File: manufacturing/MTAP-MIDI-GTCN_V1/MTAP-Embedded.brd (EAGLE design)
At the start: 160 x 100 mm, 32 parts, among them IC1 ESP32-WROOM-32D, IC2 AMS1117-3.3, X1 USB4140-GF-0230-C

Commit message: upd Embedded
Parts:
- added R11: 0R, rcl_GruS:R0805
- IC1: value ESP32-WROOM-32D -> ESP32-WROOM-32UE-N8; device modul_GruS:ESP32WROOM32D4MBPS -> modul_GruS:ESP32WROOM32UEN8
- R7: value (none) -> 47k5
- R8: value (none) -> 22k1
- S1, S2: device switch_GruS:STS6X -> switch_GruS:WE_436331045822
- moved H1 33.4 mm to (51.1, 46.0), turned to 270 degrees
- moved R1 29.7 mm to (47.3, 46.0)
- moved S2 23.9 mm to (37.5, 54.0), turned to 180 degrees
- moved C6 17.1 mm to (32.4, 53.3), flipped to the bottom, turned to 270 degrees
- moved C3 17.0 mm to (44.8, 14.0), flipped to the bottom, turned to 270 degrees
- moved C7 16.9 mm to (41.3, 49.8), flipped to the bottom, turned to 180 degrees
- moved S1 16.9 mm to (37.5, 54.0), flipped to the bottom, turned to 180 degrees
- moved C4 12.0 mm to (47.3, 14.0), flipped to the bottom
- moved V3 10.2 mm to (44.1, 40.0), turned to 270 degrees
- moved D2 8.58 mm to (44.1, 43.5), turned to 90 degrees
- moved C2 8.31 mm to (47.3, 43.2), turned to 0 degrees
- moved C1 8.26 mm to (51.1, 43.2), turned to 0 degrees
- moved R7 8.11 mm to (28.3, 44.5), turned to 90 degrees
- moved R3 7.55 mm to (40.6, 39.1), turned to 0 degrees
- moved IC2 7.31 mm to (49.2, 37.8)
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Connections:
- net GND: now also R11.2
- net PGND: now also R11.1
- net USB_DN: now also D4.1, X1.B5; no longer D3.1, X1.A5
- net USB_DP: now also D3.1, X1.A5; no longer D4.1, X1.B5
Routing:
- net +3V3: track 18.1 -> 70.8 mm
- net EN: track 6.68 -> 54.0 mm, vias 0 -> 4
- net GPIO0: track 4.32 -> 29.8 mm, vias 0 -> 1
- net VBUS: track 5.50 -> 29.7 mm
- net GND: track 14.1 -> 24.1 mm, vias 0 -> 13
- net USB_DP: track 3.85 -> 13.0 mm
- net RTS: track 3.24 -> 10.6 mm
- net N$16: track 10.0 -> 3.18 mm, vias 2 -> 0
- net RXD: track 12.6 -> 5.84 mm
- net TXD: track 14.9 -> 9.44 mm
- net RXD0: track 32.2 -> 26.8 mm, vias 2 -> 0
- net USB_DN: track 8.80 -> 13.6 mm
- net TXD0: track 29.7 -> 25.0 mm
- net N$4: track 4.59 -> 0.00 mm
- net DTR: track 21.7 -> 17.5 mm
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- added copper zone on layer 16, net GND
- added copper zone on layer 16, net PGND
- removed copper zone on layer 16, net +3V3
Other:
- board outline removed

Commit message: upd embedded schematic
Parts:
- moved R7 3.86 mm to (32.1, 45.1)
- moved C6 3.55 mm to (33.0, 49.8), turned to 180 degrees
- moved C3 1.31 mm to (44.5, 15.2), turned to 90 degrees
- moved C4 1.31 mm to (47.0, 15.2), turned to 90 degrees
- moved R10 0.63 mm to (33.0, 41.9)
- moved C8 0.32 mm to (36.5, 49.2)
- moved C9 0.32 mm to (34.3, 49.2)
- moved R8 0.32 mm to (32.1, 49.2)
- moved R9 0.32 mm to (34.3, 45.1)
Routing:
- net N$2: track 0.00 -> 6.67 mm
- net VBUS: track 29.7 -> 33.4 mm
- net N$3: track 0.00 -> 2.78 mm
- net +5V: track 6.37 -> 8.91 mm
- net GPIO0: track 29.8 -> 27.7 mm
- net PGND: track 3.40 -> 5.40 mm, vias 11 -> 32
- net N$4: track 0.00 -> 1.93 mm
- net +3V3: track 70.8 -> 72.6 mm
- net GND: vias 13 -> 15
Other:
- board outline added: 37.5 x 44.5 mm

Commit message: upd board
upd pcb
added Kostenrechnung
upd PPL-GruS
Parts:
- moved C3 11.8 mm to (56.2, 15.9), flipped to the top
- moved R11 9.40 mm to (58.4, 36.8)
- moved C4 7.01 mm to (54.0, 15.9), flipped to the top
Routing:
- net GND: track 24.1 -> 9.27 mm, vias 15 -> 14
- net EN: track 53.6 -> 58.6 mm
- net +3V3: track 72.6 -> 71.5 mm, vias 5 -> 4
- net PGND: vias 32 -> 25
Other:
- board size 37.5 x 44.5 mm -> 35.2 x 44.5 mm

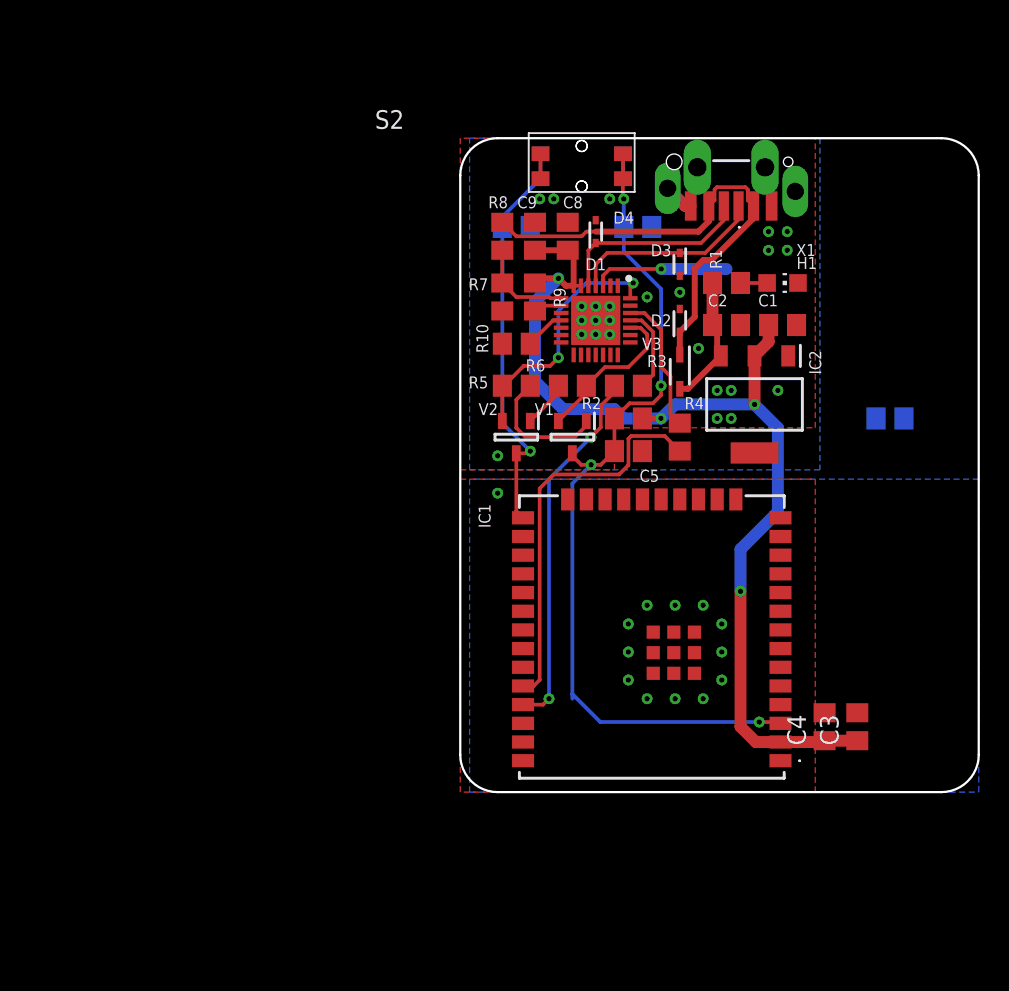
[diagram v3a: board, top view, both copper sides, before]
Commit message: Update Embedded
added PCM ADC to PCB
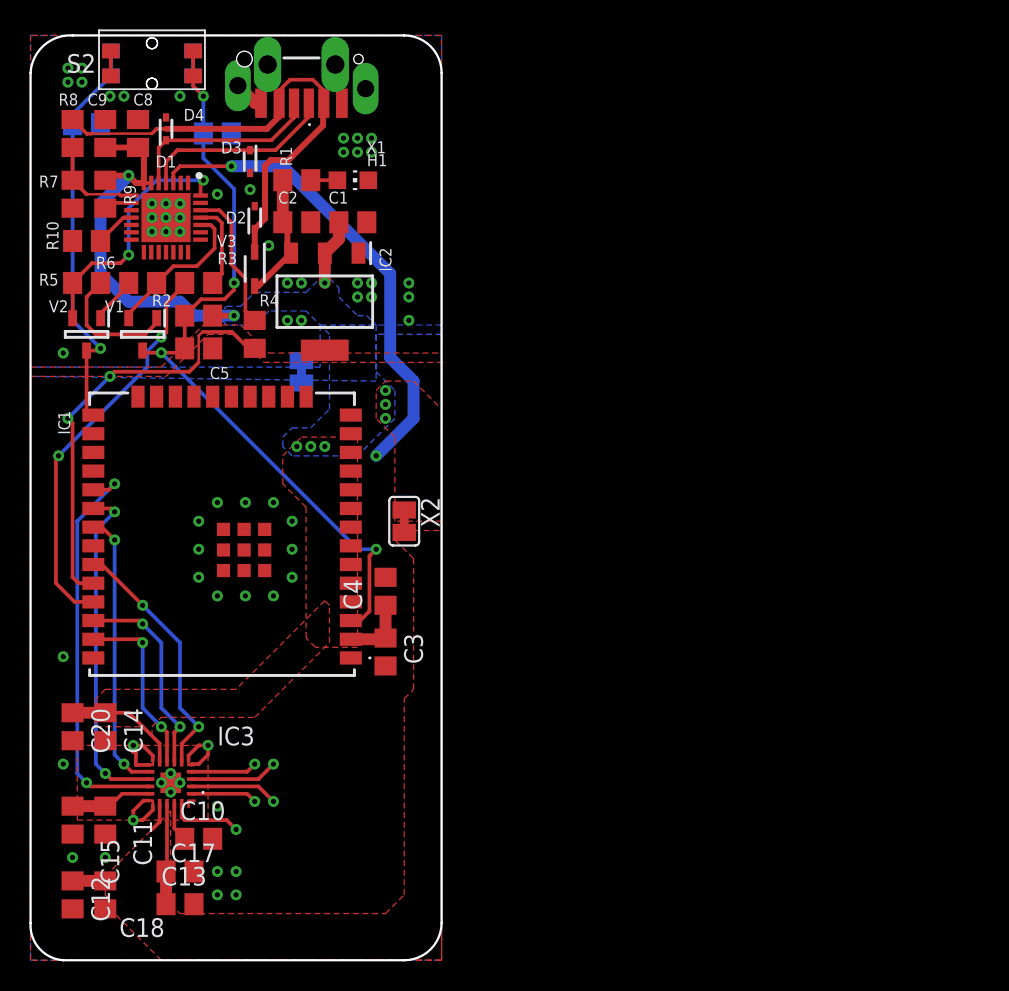
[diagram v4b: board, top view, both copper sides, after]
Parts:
- added C10, C12: 1u, rcl_GruS:C0805
- added C11, C13, C14: 10u, rcl_GruS:C0805
- added C15, C17, C18, C20: 100n, rcl_GruS:C0805
- added IC3: PCM1821IRTER, adc-dac_GruS:WQFN20
- added X2: (no value), con_GruS:MYLIB_SJ-SHORT
- C3, C5: value (none) -> 100n/50V
- C6, C7: value (none) -> 100n
- R10, R2, R5, R6: value (none) -> 10k
- R11: device rcl_GruS:R0805 -> con_GruS:MYLIB_SJ-SHORT
- R3, R4: value (none) -> 0R
- R9: value (none) -> 2k
- moved R11 40.1 mm to (18.4, 40.0), turned to 270 degrees
- moved C3 32.5 mm to (24.1, 21.0), turned to 270 degrees
- moved C4 31.2 mm to (24.1, 25.1)
- moved C6 30.0 mm to (3.81, 56.8)
- moved R10 30.0 mm to (3.81, 48.9)
- moved R5 30.0 mm to (3.81, 46.0)
- moved V2 30.0 mm to (3.81, 42.5)
- moved C1 30.0 mm to (21.9, 50.2)
- moved C5 30.0 mm to (11.4, 41.6)
- moved C8 30.0 mm to (7.30, 56.2)
- moved C9 30.0 mm to (5.08, 56.2)
- moved D3 30.0 mm to (14.9, 54.3)
- moved H1 30.0 mm to (21.9, 53.0)
- moved IC1 30.0 mm to (13.0, 29.2)
- moved R2 30.0 mm to (11.4, 43.8)
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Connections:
- new net AVDD: C12.1, C18.1, IC3.16, X2.2
- new net BCLK: IC1.36, IC3.7
- new net FSYNC: IC1.37, IC3.8
- new net FTM0: IC3.19
- new net GPIO12: IC1.14
- new net GPIO13: IC1.16
- new net GPIO14: IC1.13
- new net GPIO15: IC1.23
- new net GPIO16: IC1.27
- new net GPIO17: IC1.28
- new net GPIO2: IC1.24
- new net GPIO25: IC1.10
- new net GPIO26: IC1.11
- new net GPIO27: IC1.12
- new net GPIO32: IC1.8
- new net GPIO33: IC1.9
- new net GPIO34: IC1.6
- new net GPIO35: IC1.7
- new net GPIO4: IC1.26
- new net IN1M: IC3.2
- new net IN1P: IC3.1
- new net IN2M: IC3.4
- new net IN2P: IC3.3
- new net MD0: IC1.30, IC3.12
- new net MD1: IC1.31, IC3.11
- new net MSZ: IC1.29, IC3.13
- new net N$13: C11.1, C15.1, IC3.14
- new net N$17: C13.1, C17.1, IC3.17
- new net N$9: C10.1, IC3.18
- new net SDATA: IC1.33, IC3.6
- net +3V3: now also C14.1, C20.1, IC3.9, X2.1
- net GND: now also C10.2, C11.2, C12.2, C13.2, C14.2, C15.2, C17.2, C18.2, C20.2, IC3.10, IC3.15, IC3.20, IC3.21, IC3.22, IC3.23, IC3.24, IC3.25, IC3.5
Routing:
- net GND: track 9.27 -> 45.2 mm, vias 14 -> 30
- net MSZ: track 0.00 -> 27.7 mm, vias 0 -> 2
- net +3V3: track 71.5 -> 44.7 mm, vias 4 -> 9
- net MD0: track 0.00 -> 23.3 mm, vias 0 -> 2
- net MD1: track 0.00 -> 19.3 mm, vias 0 -> 2
- net SDATA: track 0.00 -> 17.2 mm, vias 0 -> 2
- net BCLK: track 0.00 -> 14.1 mm, vias 0 -> 2
- net FSYNC: track 0.00 -> 12.3 mm, vias 0 -> 2
- net N$17: track 0.00 -> 6.88 mm
- net IN2P: track 0.00 -> 6.01 mm, vias 0 -> 1
- net IN1M: track 0.00 -> 6.01 mm, vias 0 -> 1
- net EN: track 58.6 -> 52.9 mm
- net N$13: track 0.00 -> 5.62 mm
- net FTM0: track 0.00 -> 4.98 mm, vias 0 -> 1
- net IN2M: track 0.00 -> 4.53 mm, vias 0 -> 1
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- added copper zone on layer 1, net +3V3
- added copper zone on layer 16, net +3V3
- added copper zone on layer 1, net AVDD
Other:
- board size 35.2 x 44.5 mm -> 27.9 x 62.9 mm

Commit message: Upd pcb
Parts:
- moved D3 0.32 mm to (15.2, 54.3)
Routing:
- net +3V3: track 44.7 -> 43.1 mm
- net GND: track 45.2 -> 46.4 mm

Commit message: upd analog board
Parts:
- added C16, C21: 10n, rcl_GruS:C0805
- added C19: 680n, rcl_GruS:C0805
- added R12: 6k2, rcl_GruS:R0805
- added R13: 2k4, rcl_GruS:R0805
- added R14: 240, rcl_GruS:R0805
- added R15: 5k1, rcl_GruS:R0805
- added R16: 200, rcl_GruS:R0805
- added R17: 750, rcl_GruS:R0805
- added V4: TLV9354IPWR, opv_GruS:SOP65P640X120-14N
- added X3: (no value), con-lstb:MA02-1
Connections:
- removed net GPIO17: IC1.28
- new net N$10: R14.1, R15.2, V4.14
- new net N$11: C21.2, R16.2, V4.10
- new net N$5: R12.1, X3.2
- new net N$6: C16.1, R12.2, V4.12
- new net N$7: R13.2, R15.1, V4.13
- new net N$8: C19.1, R14.2, R16.1, R17.1
- net AVDD: now also V4.4
- net FTM0: now also IC1.28
- net GND: now also C16.2, C19.2, R13.1, V4.11, V4.9, X3.1
- net IN1P: now also C21.1, R17.2, V4.8
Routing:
- net FTM0: track 4.98 -> 34.8 mm, vias 1 -> 2
- net IN2P: track 6.01 -> 0.00 mm, vias 1 -> 0
- net IN1M: track 6.01 -> 0.00 mm, vias 1 -> 0
- net IN2M: track 4.53 -> 0.00 mm, vias 1 -> 0
- net IN1P: track 4.53 -> 0.00 mm, vias 1 -> 0
- net GND: track 46.4 -> 50.8 mm

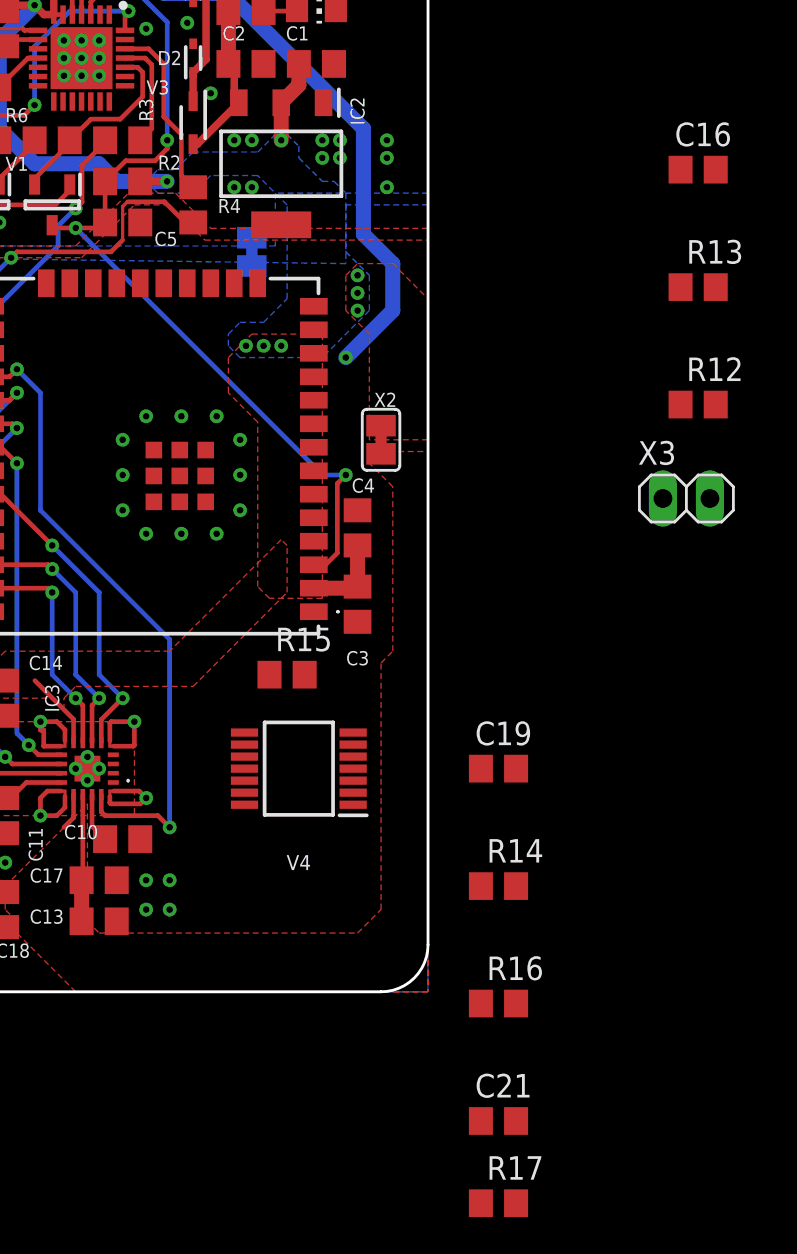
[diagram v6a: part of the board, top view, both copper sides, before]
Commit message: upd pcb
added filter to schematic
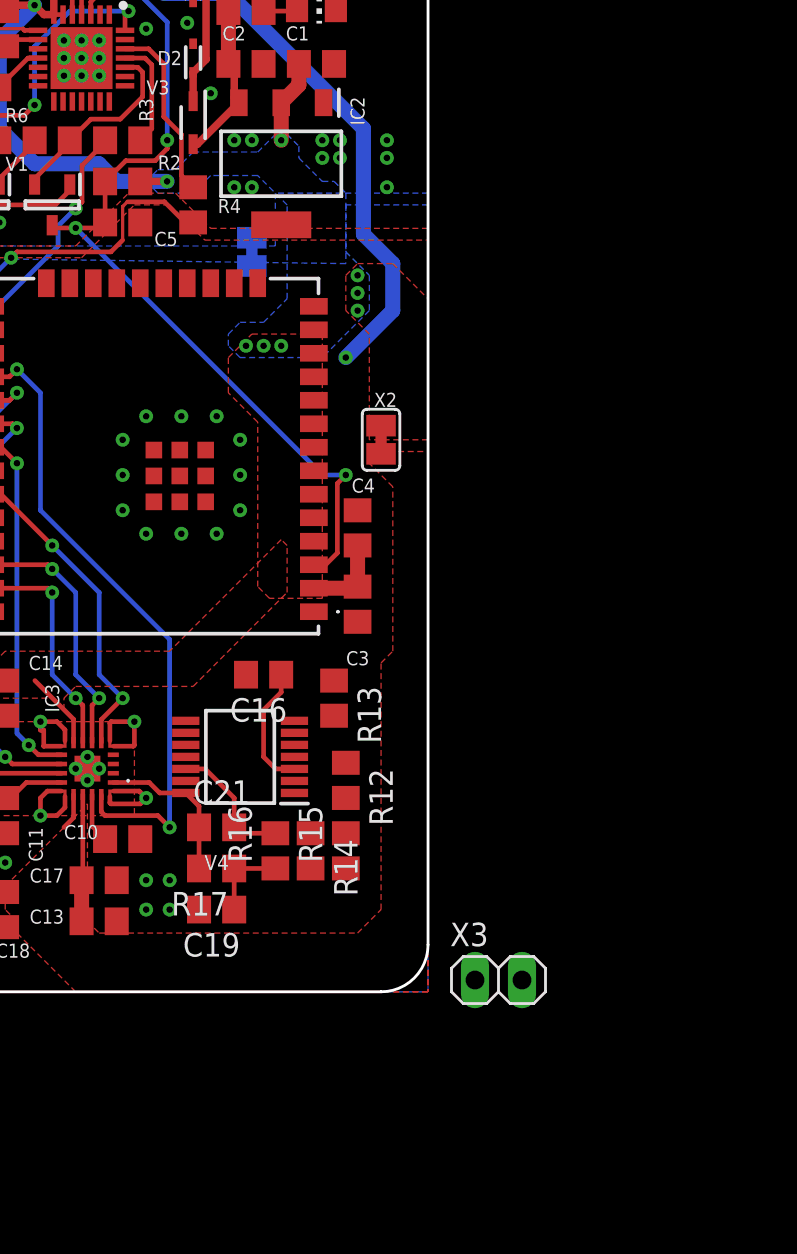
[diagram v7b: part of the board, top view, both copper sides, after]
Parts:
- moved C16 36.0 mm to (19.1, 17.1), turned to 180 degrees
- moved R13 29.7 mm to (22.9, 15.9), turned to 270 degrees
- moved X3 27.9 mm to (31.8, 0.64)
- moved R12 27.9 mm to (23.5, 11.4), turned to 270 degrees
- moved R17 23.7 mm to (16.5, 6.67), turned to 180 degrees
- moved C21 22.0 mm to (16.5, 8.89)
- moved C19 17.0 mm to (16.5, 4.45), turned to 180 degrees
- moved R16 14.6 mm to (19.7, 7.62), turned to 90 degrees
- moved R14 10.3 mm to (21.6, 7.62), turned to 270 degrees
- moved R15 10.0 mm to (23.5, 7.62), turned to 90 degrees
- moved V4 3.24 mm to (17.8, 12.7)
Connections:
- net GND: now also V4.10, V4.13, V4.5, V4.6
- net IN1P: now also V4.14; no longer V4.8
- net N$10: now also V4.1; no longer V4.14
- net N$11: now also V4.12; no longer V4.10
- net N$6: now also V4.3; no longer V4.12
- net N$7: now also V4.2; no longer V4.13
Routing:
- net IN1P: track 0.00 -> 8.53 mm
- net N$11: track 0.00 -> 7.22 mm
- net N$6: track 0.00 -> 6.78 mm
- net N$8: track 0.00 -> 4.45 mm

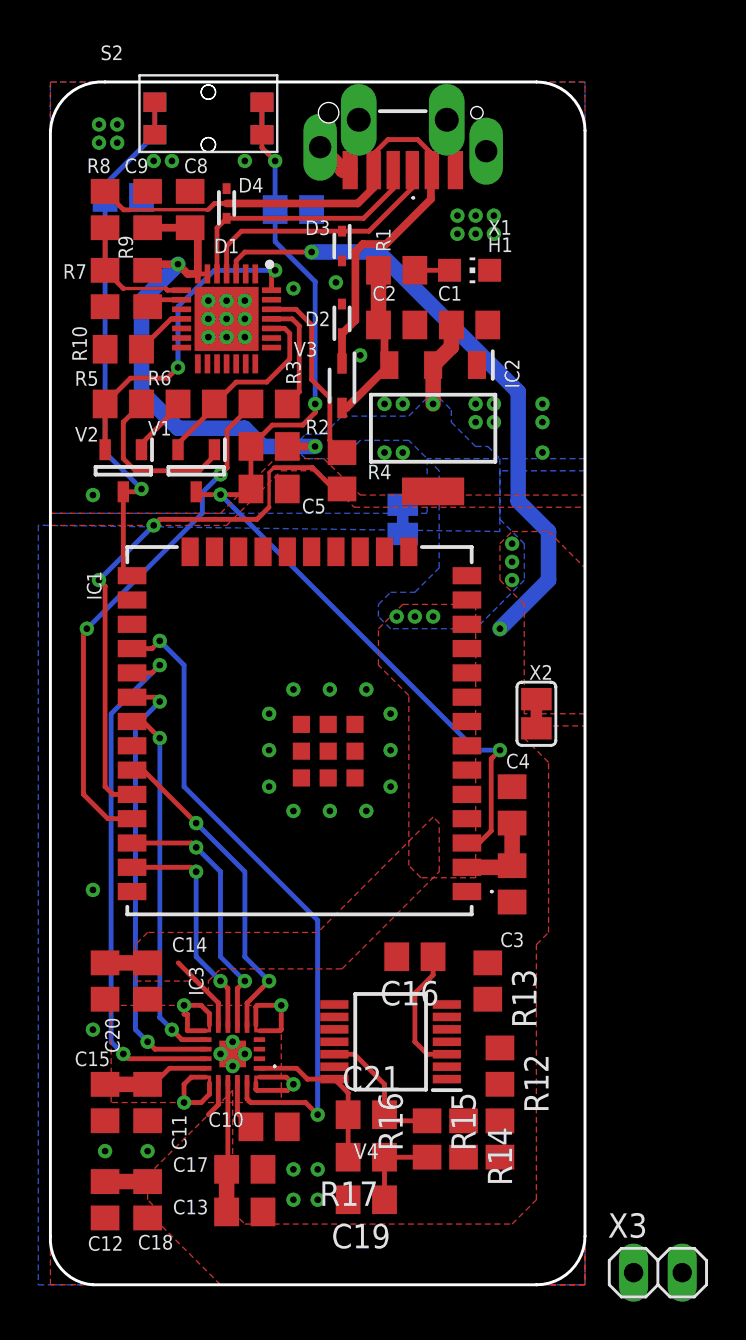
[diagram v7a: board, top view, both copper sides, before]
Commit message: ADC unavailable PCB upd
#3 Issued.
Last Push before replacement.
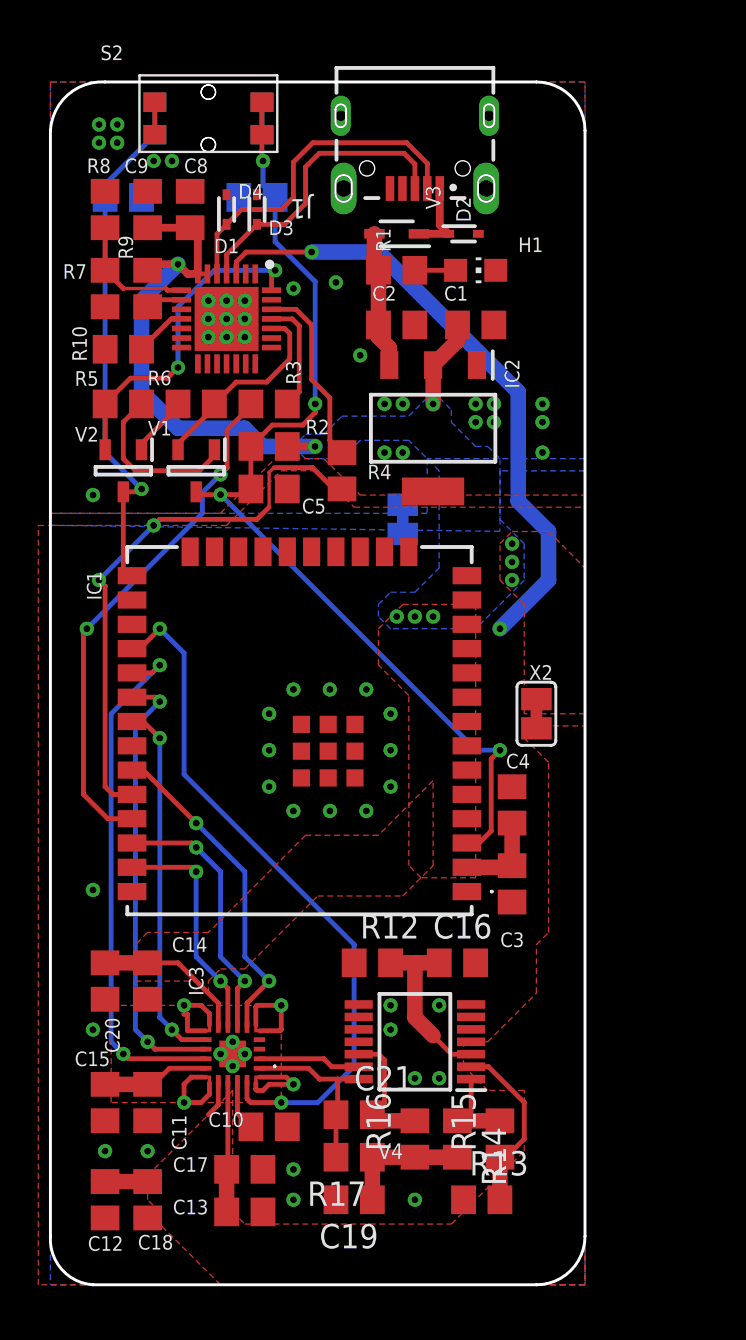
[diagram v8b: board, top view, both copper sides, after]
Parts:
- removed X1: USB4140-GF-0230-C, con_GruS:USB4140GF0230C
- removed X3: (no value), con-lstb:MA02-1
- added J1: 629105150521, Wurth_Connectors_WR-USB:629105150521
- moved R13 11.4 mm to (22.5, 4.45), turned to 0 degrees
- moved R12 8.58 mm to (16.8, 16.8), turned to 0 degrees
- moved V3 8.44 mm to (18.1, 54.9), turned to 180 degrees
- moved D2 7.75 mm to (21.6, 54.9), turned to 0 degrees
- moved D3 4.84 mm to (10.8, 56.2), turned to 90 degrees
- moved C16 2.25 mm to (21.3, 16.8), turned to 0 degrees
- moved C7 2.01 mm to (10.8, 56.8), turned to 0 degrees
- moved V4 1.27 mm to (19.1, 12.7)
- moved C19 0.64 mm to (15.9, 4.45)
- moved C21 0.64 mm to (15.9, 8.89)
- moved R17 0.64 mm to (15.9, 6.67)
- moved R16 0.63 mm to (19.1, 7.62)
- moved C1 0.32 mm to (22.2, 50.2)
- moved D4 0.32 mm to (9.21, 56.2)
- moved H1 0.32 mm to (22.2, 53.0)
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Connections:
- removed net IN1M: IC3.2
- net GND: now also IC3.2; no longer X3.1
- net N$5: no longer X3.2
- net PGND: now also J1.5, J1.S1, J1.S2, J1.S3, J1.S4; no longer X1.A12, X1.B12, X1.MH1, X1.MH2, X1.MH3, X1.MH4
- net USB_DN: now also J1.2; no longer X1.B5
- net USB_DP: now also J1.3; no longer X1.A5
- net VBUS: now also J1.1; no longer X1.A9, X1.B9
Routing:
- net VBUS: track 34.0 -> 4.12 mm
- net N$7: track 0.00 -> 9.35 mm
- net GND: track 50.8 -> 56.1 mm, vias 30 -> 34
- net N$10: track 0.00 -> 4.80 mm
- net USB_DN: track 13.4 -> 17.9 mm
- net N$6: track 6.78 -> 9.14 mm
- net USB_DP: track 13.4 -> 15.7 mm
- net N$8: track 4.45 -> 6.67 mm
- net PGND: track 5.40 -> 3.40 mm, vias 37 -> 30
- net +3V3: track 43.1 -> 44.8 mm
- net FTM0: track 34.8 -> 36.4 mm
- net +5V: track 8.59 -> 7.18 mm
- net IN1P: track 8.53 -> 9.54 mm
